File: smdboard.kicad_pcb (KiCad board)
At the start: 2 copper layers, 50 x 50 mm, 164 parts, among them IC1 4017, IC2 555, IC3 STM32F091RxHx, J1 MICROUSB, P1 SWD_TC, X1 MSOP-8, X3 LQFP-48, X4 QFN-48, X9 LQFP-100

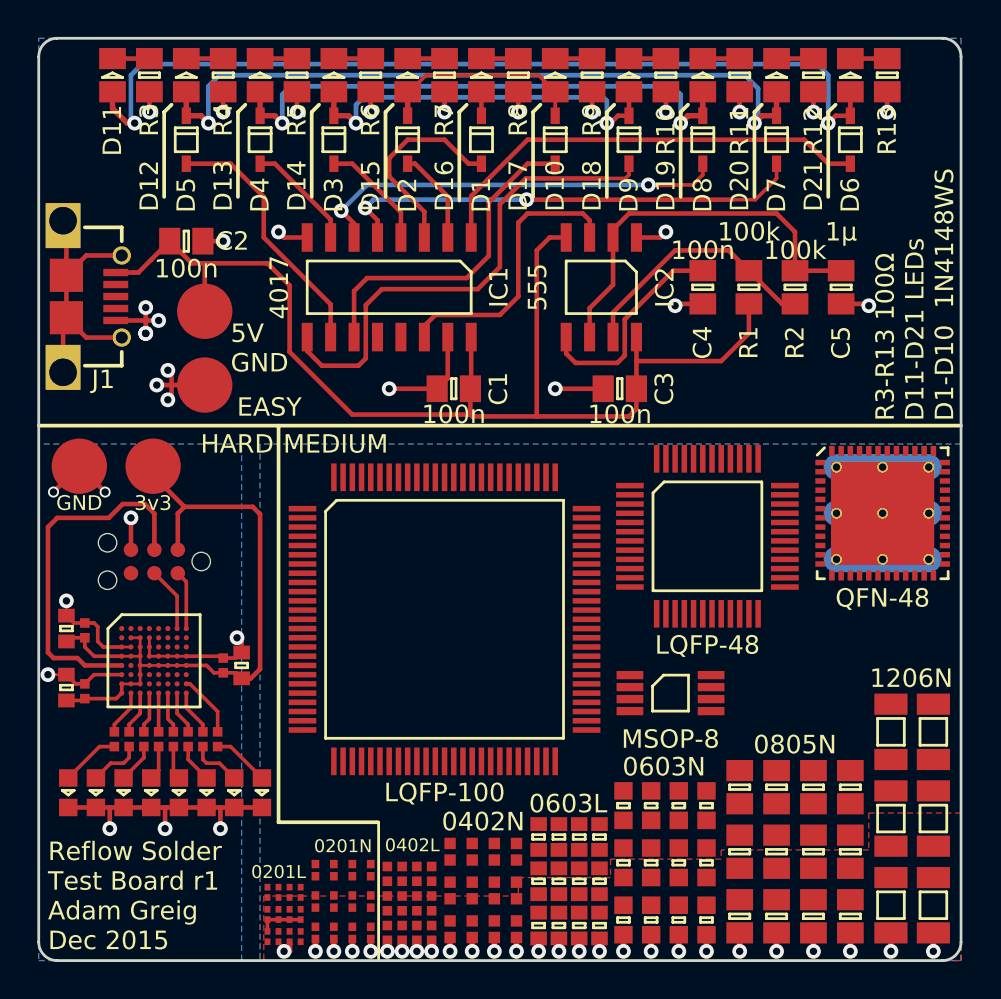
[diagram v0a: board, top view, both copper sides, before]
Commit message: Update USB and QFN-48 parts. Redraw gerbers.
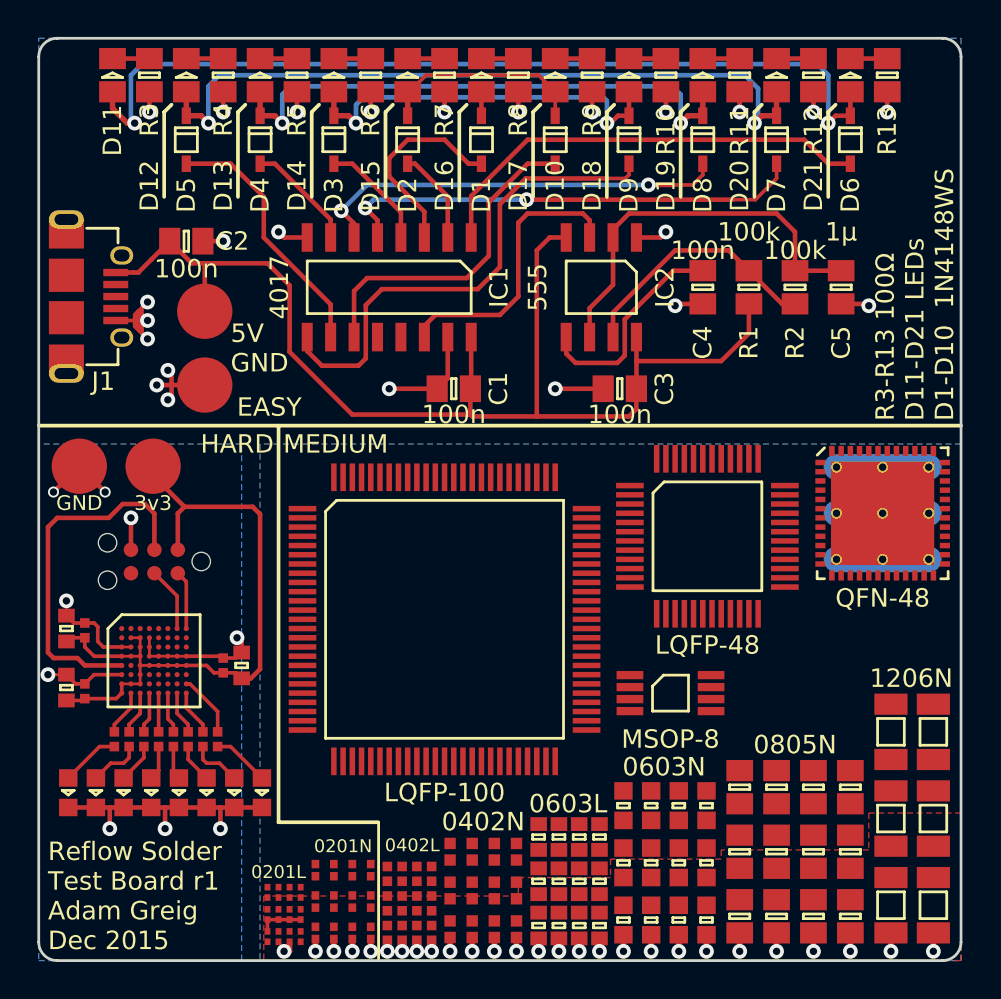
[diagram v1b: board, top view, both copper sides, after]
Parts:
- turned J1 to 270 degrees
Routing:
- net Net-(J1-PadS): track 15.3 -> 0.00 mm
- net GND: track 36.3 -> 40.2 mm, vias 25 -> 24
